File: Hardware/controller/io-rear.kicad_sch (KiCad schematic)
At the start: 14 parts

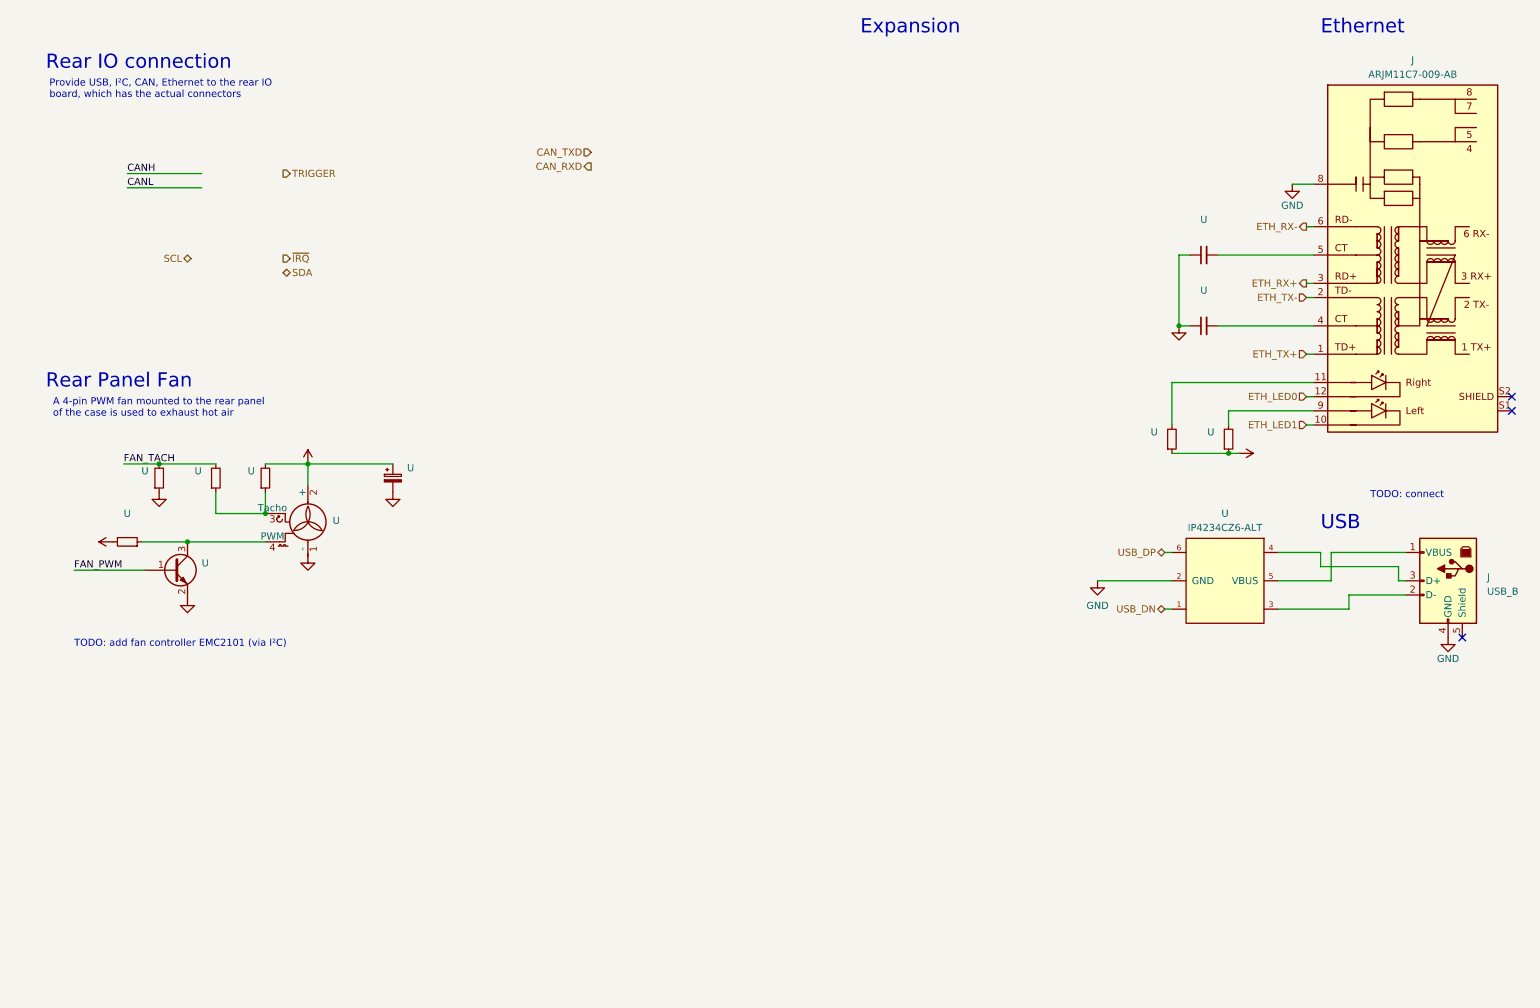
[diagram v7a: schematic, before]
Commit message: Work on Ethernet stuff
- Placed the Ethernet PHY, and some of its required
  capcacitors/resistors, including some modifications to the LEDs and
  connections on the magjack

- Minor power supply tweaks

- Added footprint for a 4 position pluggable terminal, to use for rear
  IO for expansion
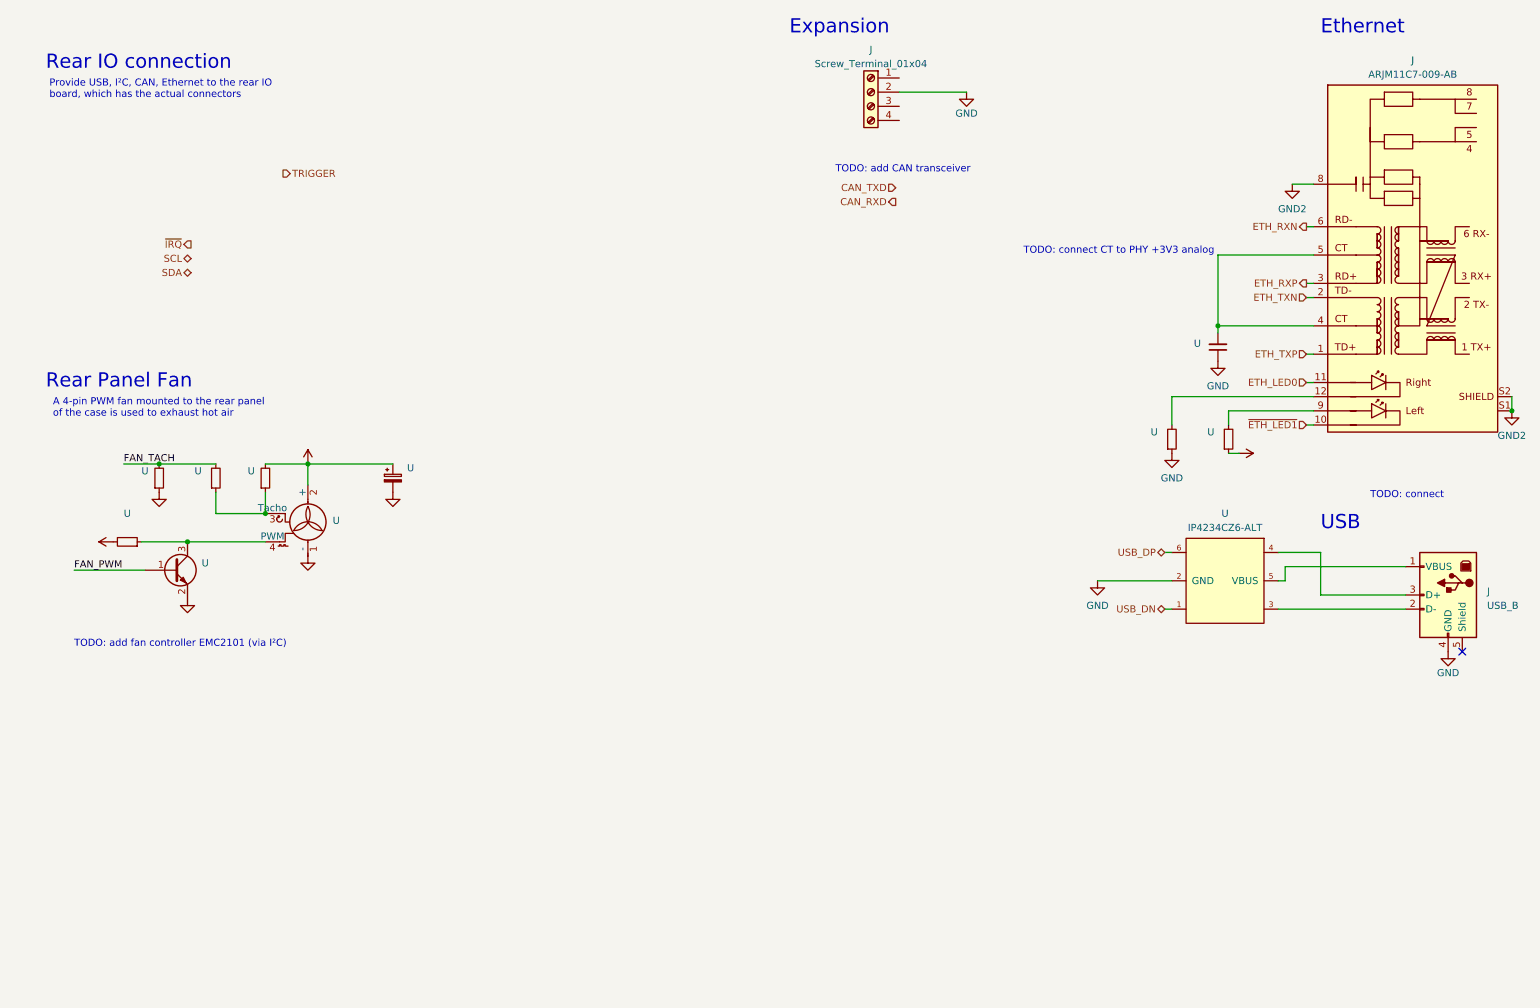
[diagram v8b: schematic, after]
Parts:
- removed U: (no value), symbol Device:C_Small
- added J: Screw_Terminal_01x04, symbol Connector:Screw_Terminal_01x04
- U: MPN CL21B104KACNFNC -> CL21B223KBANNND
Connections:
- net +3V3: no longer U.1
- net ETH_LED0: now also J.11 (LLED+); no longer J.12 (LLED-)
- net GND: now also U.1, J.2 (Pin_2); no longer J.8
- net at U.2: now also J.12 (LLED-); no longer J.11 (LLED+)
- net at J.5 (CT): now also J.4 (CT), U.2
- net GND2: now reaches J.S1 (SHIELD)
- net GND2: now also J.8, J.S2 (SHIELD)
- net ETH_LED1 renamed ~{ETH_LED1}
- net ETH_RX+ renamed ETH_RXP
- net ETH_RX- renamed ETH_RXN
- net ETH_TX+ renamed ETH_TXP
- net ETH_TX- renamed ETH_TXN
- no-connect marks 3 -> 1
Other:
- note added: "TODO: add CAN transceiver"
- note added: "TODO: connect CT to PHY +3V3 analog"
- moved on the sheet: J, U
